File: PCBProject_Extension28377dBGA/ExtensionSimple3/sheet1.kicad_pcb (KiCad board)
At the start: 4 copper layers, 140.3 x 101.7 mm, 114 parts, among them J1 Conn_02x05_Odd_Even, J2 Conn_01x02_Pin, J3 Conn_01x02_Pin, J4 Conn_01x02_Pin, J5 Conn_01x02_Pin, J6 Conn_02x05_Odd_Even, Q1 FMMT618TA, U1 SN74ABT541, U2 SN74ABT541

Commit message: fix some extension bugs
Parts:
- DI1, POWER1: moved to B.Cu
- moved CAN_A1 21.7 mm to (191.9, 68.7)
- moved R44 7.15 mm to (316.9, 122.5), turned to 0 degrees
- moved R34 5.99 mm to (313.3, 122.5), turned to 0 degrees
- moved J4 5.05 mm to (311.0, 128.6), turned to 90 degrees
- moved SPI-DAC2 3.39 mm to (197.8, 148.0)
- moved UART4 3.22 mm to (235.4, 158.4)
- moved CAN_B1 2.99 mm to (212.1, 68.7)
- moved DI1 2.55 mm to (207.5, 133.3), turned to 0 degrees
- moved POWER1 2.46 mm to (197.7, 95.0), turned to 180 degrees
- moved J1 2.25 mm to (232.4, 69.6)
- moved UART3 2.15 mm to (246.9, 158.4)
- moved VDC_BUS1 1.82 mm to (298.8, 134.2)
- moved D1 1.53 mm to (295.3, 134.2)
- moved D4 1.50 mm to (306.9, 133.5)
- moved VDC_BUS3 1.44 mm to (302.9, 134.2)
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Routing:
- net VDD: track 267.5 -> 294.2 mm
- net /DSP_A_CAN_TX: track 15.6 -> 38.9 mm
- net /DSP_A_CAN_RX: track 17.7 -> 40.9 mm
- net PE_GND: track 176.0 -> 187.8 mm
- net D12V1: track 344.8 -> 356.6 mm
- net AVDD: track 273.6 -> 284.2 mm
- net /UART_SCI_WRC: track 17.5 -> 27.0 mm
- net A+5V: track 318.0 -> 325.5 mm
- net /GND_2M4: track 9.31 -> 16.5 mm
- net /UART_SCI_WRB: track 23.6 -> 30.4 mm
- net /MQEP1Z: track 24.8 -> 30.6 mm
- net /MQEP1B: track 24.3 -> 28.8 mm
- net Net-(C14-Pad1): track 8.27 -> 12.6 mm
- net /UART_SCI_RXDD: track 22.3 -> 25.5 mm
- net /DSP_B_CAN_TX: track 29.4 -> 26.2 mm
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
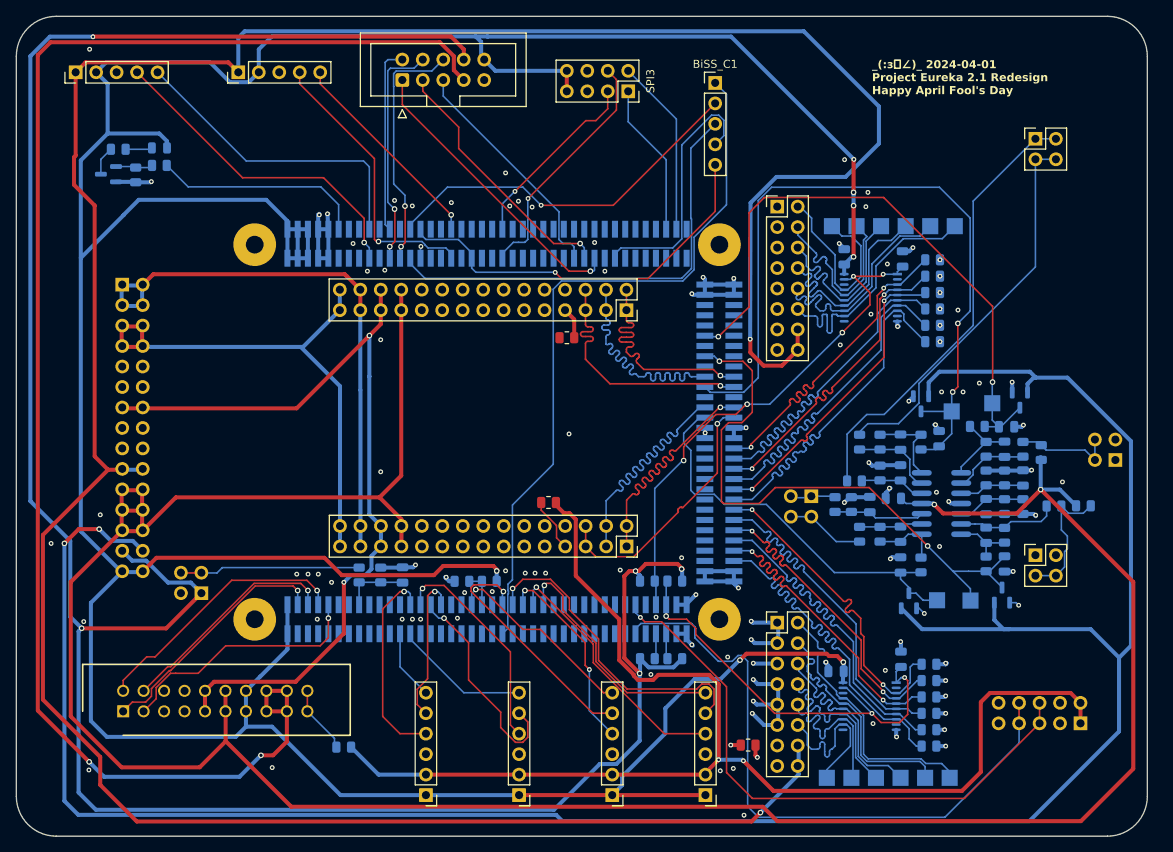
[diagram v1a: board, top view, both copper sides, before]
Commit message: let VDD to 485
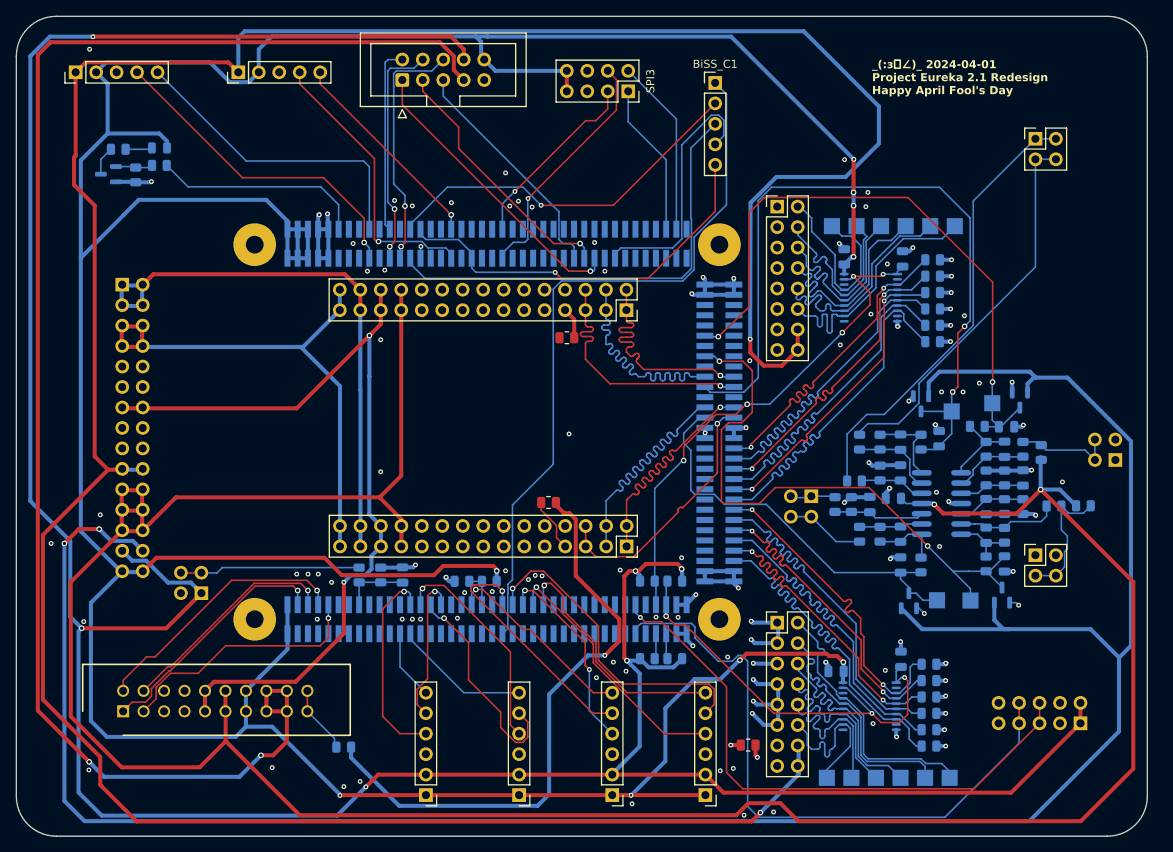
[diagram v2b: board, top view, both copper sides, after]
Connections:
- J6 pad 1: REF_3V -> VDD
- J6 pad 2: REF_3V -> VDD
- UART1 pad 2: REF_3V -> VDD
- UART2 pad 2: REF_3V -> VDD
- UART3 pad 2: REF_3V -> VDD
- UART4 pad 2: REF_3V -> VDD
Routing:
- net REF_3V: track 154.1 -> 73.5 mm, vias 2 -> 1
- net VDD: track 294.2 -> 360.6 mm, vias 5 -> 6
- net AGND: track 137.3 -> 145.5 mm, vias 112 -> 119
- net /IPM_VDC_BUS3: track 76.2 -> 78.0 mm
- net A+5V: track 325.5 -> 326.8 mm
- net /MSCLA: track 73.3 -> 72.4 mm
- net D+5V: track 469.2 -> 468.6 mm, vias 7 -> 9

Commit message: fix VDD and ref_3V, DC_bus location
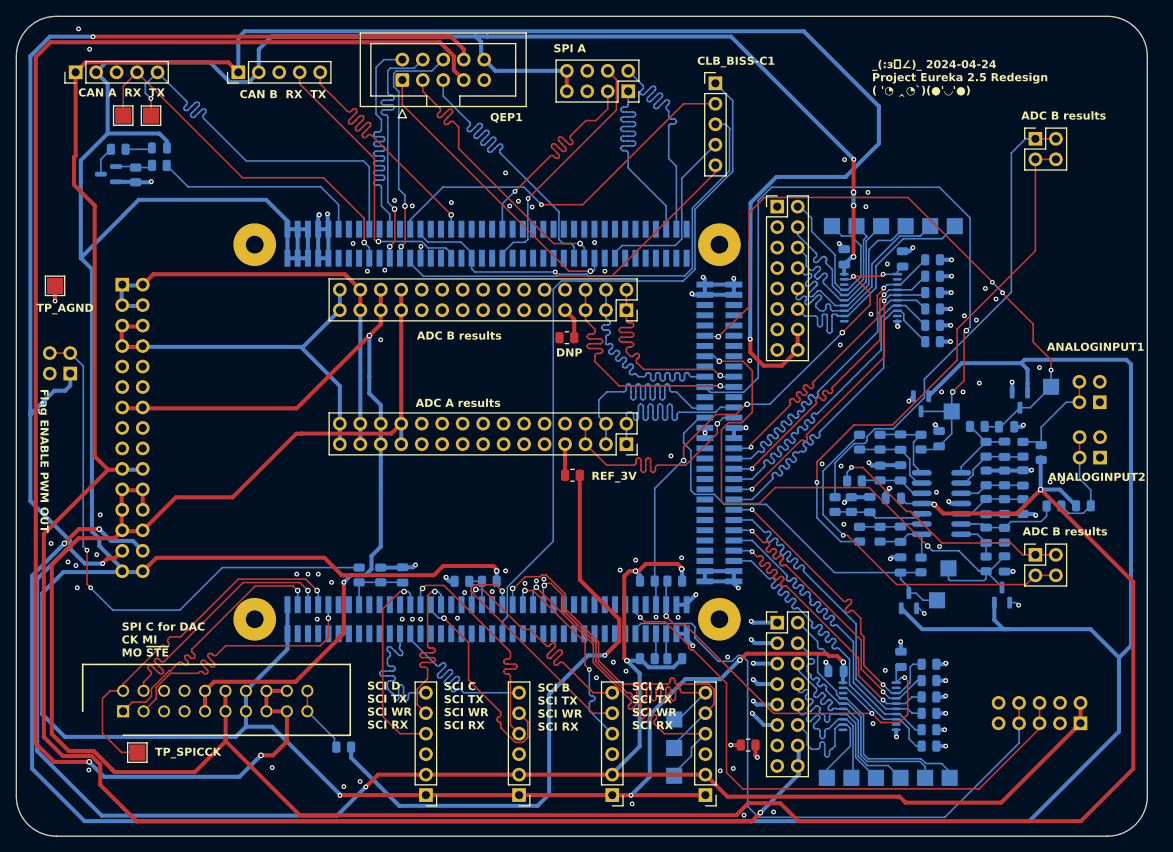
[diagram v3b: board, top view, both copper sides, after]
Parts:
- removed BiSS_C1: Conn_01x05, Connector_PinHeader_2.54mm:PinHeader_1x05_P2.54mm_Vertical
- removed VDC_BUS3, VDC_BUS4: TP-黄色测试点, TestPoint:TestPoint_Pad_2.0x2.0mm
- added ANALOGINPUT1: TP-黄色测试点, TestPoint:TestPoint_Pad_2.0x2.0mm, B.Cu at (312.9, 107.7)
- added ANALOGINPUT2: TP-黄色测试点, TestPoint:TestPoint_Pad_2.0x2.0mm, B.Cu at (300.2, 130.2)
- added CLB_BiSS_C1: Conn_01x05, Connector_PinHeader_2.54mm:PinHeader_1x05_P2.54mm_Vertical, F.Cu at (271.3, 70.0)
- added TESTPOINT1: TP-黄色测试点, TestPoint:TestPoint_Pad_2.0x2.0mm, B.Cu at (266.2, 156.0)
- added TESTPOINT2: TP-黄色测试点, TestPoint:TestPoint_Pad_2.0x2.0mm, B.Cu at (266.2, 149.0)
- added TESTPOINT3: TP-黄色测试点, TestPoint:TestPoint_Pad_2.0x2.0mm, F.Cu at (189.3, 95.2)
- added TESTPOINT4: TP-黄色测试点, TestPoint:TestPoint_Pad_2.0x2.0mm, F.Cu at (199.6, 153.1)
- added TESTPOINT5: TP-黄色测试点, TestPoint:TestPoint_Pad_2.0x2.0mm, B.Cu at (266.2, 152.5)
- added TESTPOINT6: TP-黄色测试点, TestPoint:TestPoint_Pad_2.0x2.0mm, F.Cu at (197.8, 74.0)
- added TESTPOINT7: TP-黄色测试点, TestPoint:TestPoint_Pad_2.0x2.0mm, F.Cu at (201.3, 74.0)
- J2: moved to F.Cu
- J4: moved to B.Cu
- moved J2 52.3 mm to (311.0, 76.9)
- moved J3 51.6 mm to (311.0, 128.5)
- moved DI1 31.7 mm to (191.2, 106.0)
- moved J4 14.5 mm to (319.0, 116.5), turned to 0 degrees
- moved LEM2 12.7 mm to (260.2, 114.8)
- moved J5 7.42 mm to (319.0, 109.6)
- moved RU2 4.50 mm to (253.6, 118.7)
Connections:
- net /GND_2M3 renamed Net-(J5-Pin_2)
- net /GND_2M4 renamed Net-(J4-Pin_2)
- net /IPM_VDC_BUS3 renamed /ANALOGINPUT1
- net /IPM_VDC_BUS4 renamed /ANALOGINPUT2
- net /SPICLK renamed /CLB_SPICLK
- DSP1 pad 124: /TX_DIR -> /CLB_TX_DIR
- DSP1 pad 25: /DATA_IN -> /CLB_DATA_IN
- DSP1 pad 26: /DATA_OUT -> /CLB_DATA_OUT
- DSP1 pad 66: /PWR_CTL -> /CLB_PWR_CTL
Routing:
- net /CLB_TX_DIR: track 0.00 -> 89.9 mm
- net /TX_DIR: track 89.3 -> 0.00 mm
- net /CLB_DATA_OUT: track 0.00 -> 58.2 mm
- net /GND_2M1: track 9.81 -> 67.6 mm, vias 0 -> 1
- net /DATA_OUT: track 56.1 -> 0.00 mm
- net /DC_BUS_2M1: track 5.53 -> 60.3 mm
- net Net-(DI1-Pin_3): track 22.4 -> 69.5 mm, vias 0 -> 2
- net /CLB_DATA_IN: track 0.00 -> 46.9 mm, vias 0 -> 1
- net /DATA_IN: track 46.6 -> 0.00 mm, vias 1 -> 0
- net /PWR_CTL: track 31.7 -> 0.00 mm
- net /DC_BUS_2M2: track 55.9 -> 32.0 mm, vias 0 -> 1
- net /CLB_PWR_CTL: track 0.00 -> 23.1 mm
- net /UART_SCI_TXDA: track 30.8 -> 49.6 mm
- net /UART_SCI_TXDD: track 8.65 -> 24.7 mm
- net -12: track 65.9 -> 50.7 mm
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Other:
- board text added: "ADC A results"
- board text added: "ADC B results"
- board text added: "ANALOGINPUT1"
- board text added: "ANALOGINPUT2"
- board text added: "CAN A RX TX"
- board text added: "CAN B RX TX"
- board text added: "CLB_BISS-C1"
- board text added: "DNP"
- board text added: "Flag ENABLE PWM OUT"
- board text added: "GPIO3"
- board text added: "I2C"
- board text added: "POWER"
- board text added: "PWM3B 2B 1B 3A 2A 1A"
- board text added: "PWM4A 5A 6A 4B 5B 6B"
- board text added: "QEP1"
- board text added: "REF_3V"
- board text added: "SCI A SCI TX SCI WR SCI RX"
- board text added: "SCI B SCI TX SCI WR SCI RX"
- board text added: "SCI C SCI TX SCI WR SCI RX"
- board text added: "SCI D SCI TX SCI WR SCI RX"
- board text added: "SPI A"
- board text added: "SPI C for DAC CK MI MO ~{STE}"
- board text added: "TP_AGND"
- board text added: "TP_SPICCK"
- board text added: "TP_TX WR RX"
- board text added: "_(:з」∠)_ 2024-04-24 Project Eureka 2.5 Redesign ( '◔︎ ‸◔︎`)(●'◡'●)"
- board text removed: "_(:з」∠)_ 2024-04-01 Project Eureka 2.1 Redesign Happy April Fool's Day"
